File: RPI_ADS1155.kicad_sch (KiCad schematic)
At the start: 28 parts, among them J1 Raspberry_PI_4, J2 DIGITAL_BITS, SW1 SW_DIP_x04, SW2 SW_Push, SW3 SW_Push, U1 ADS1115IDGS

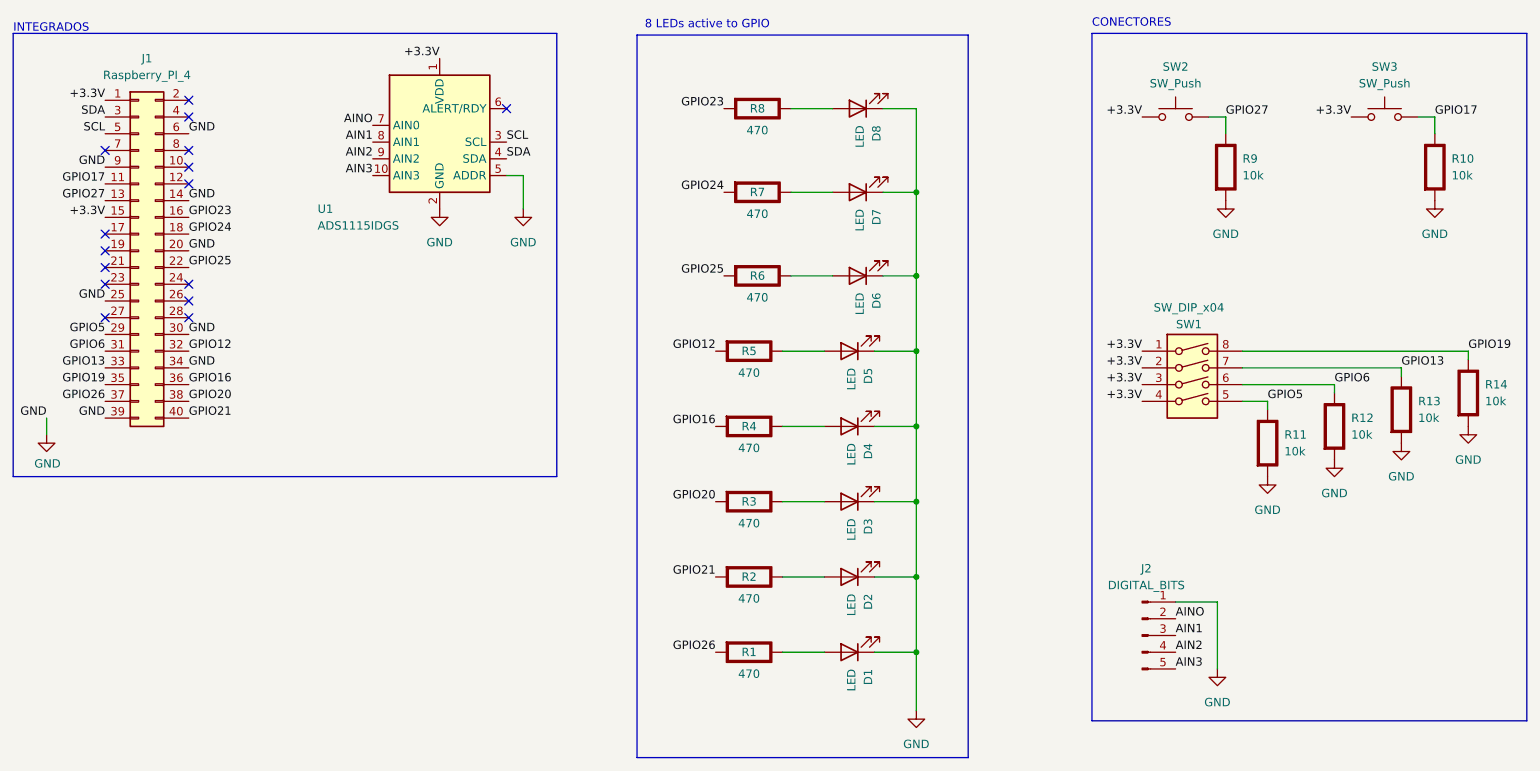
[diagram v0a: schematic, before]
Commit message: Add UART connector and pins
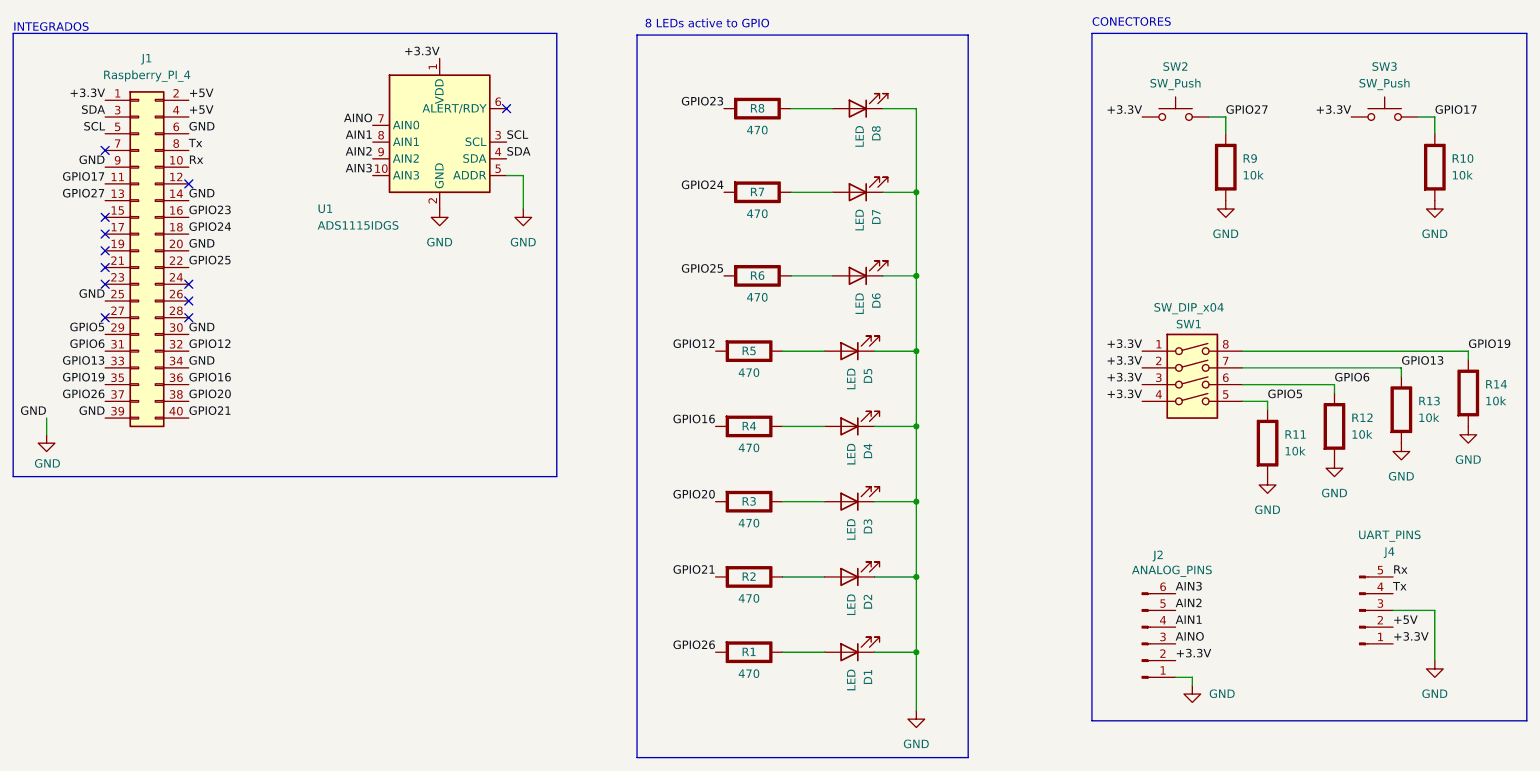
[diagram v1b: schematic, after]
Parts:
- removed J2: DIGITAL_BITS, Connector_PinHeader_2.54mm:PinHeader_1x05_P2.54mm_Vertical, symbol Connector:Conn_01x05_Pin
- added J2: ANALOG_PINS, Connector_PinSocket_2.54mm:PinSocket_1x06_P2.54mm_Vertical, symbol Connector:Conn_01x06_Pin
- added J4: UART_PINS, Connector_PinSocket_2.54mm:PinSocket_1x05_P2.54mm_Vertical, symbol Connector:Conn_01x05_Pin
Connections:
- net +3.3V: now also J2.2 (Pin_2), J4.1 (Pin_1); no longer J1.15 (Pin_15)
- net AIN1: now also J2.4 (Pin_4)
- net AIN2: now also J2.5 (Pin_5)
- net AIN3: now also J2.6 (Pin_6)
- net AINO: now also J2.3 (Pin_3)
- net GND: now also J2.1 (Pin_1), J4.3 (Pin_3)
- net Rx: now reaches J1.10 (Pin_10)
- net Rx: now also J4.5 (Pin_5)
- net +5V: now reaches J1.2 (Pin_2)
- net +5V: now also J1.4 (Pin_4), J4.2 (Pin_2)
- net Tx: now reaches J1.8 (Pin_8)
- net Tx: now also J4.4 (Pin_4)
- no-connect marks 15 -> 12
